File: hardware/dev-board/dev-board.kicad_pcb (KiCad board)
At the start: 4 copper layers, 66 x 119.3 mm, 150 parts, among them IC201 ADV7393BCPZ, J101 Conn_01x02_Pin, J102 DISC1-P1, J103 DISC1-P2, J201 CVBS, J301 Connector RGB, U101 MCP2562-E-SN, U102 CDCE913PW, U103 AMS1117-1.8, U301 ADV7125KSTZ140

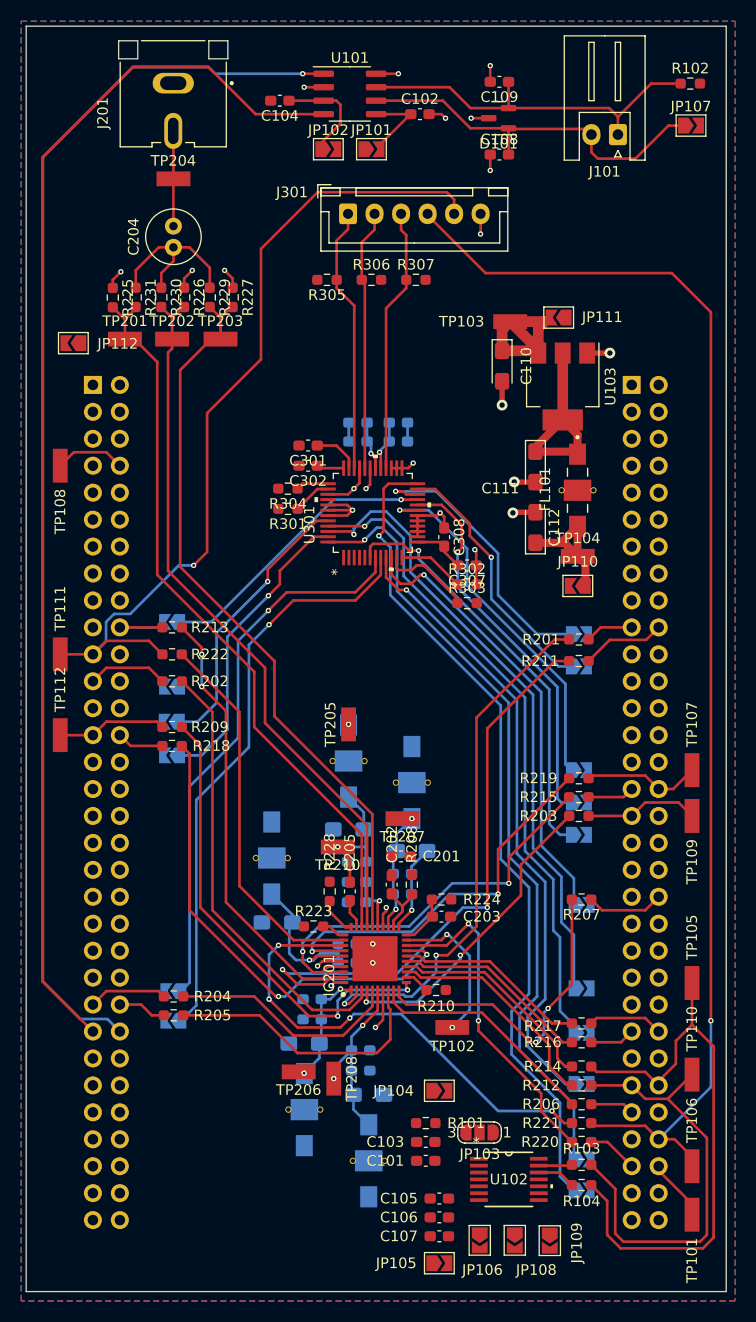
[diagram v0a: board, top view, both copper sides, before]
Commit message: adv7393 dev-board done
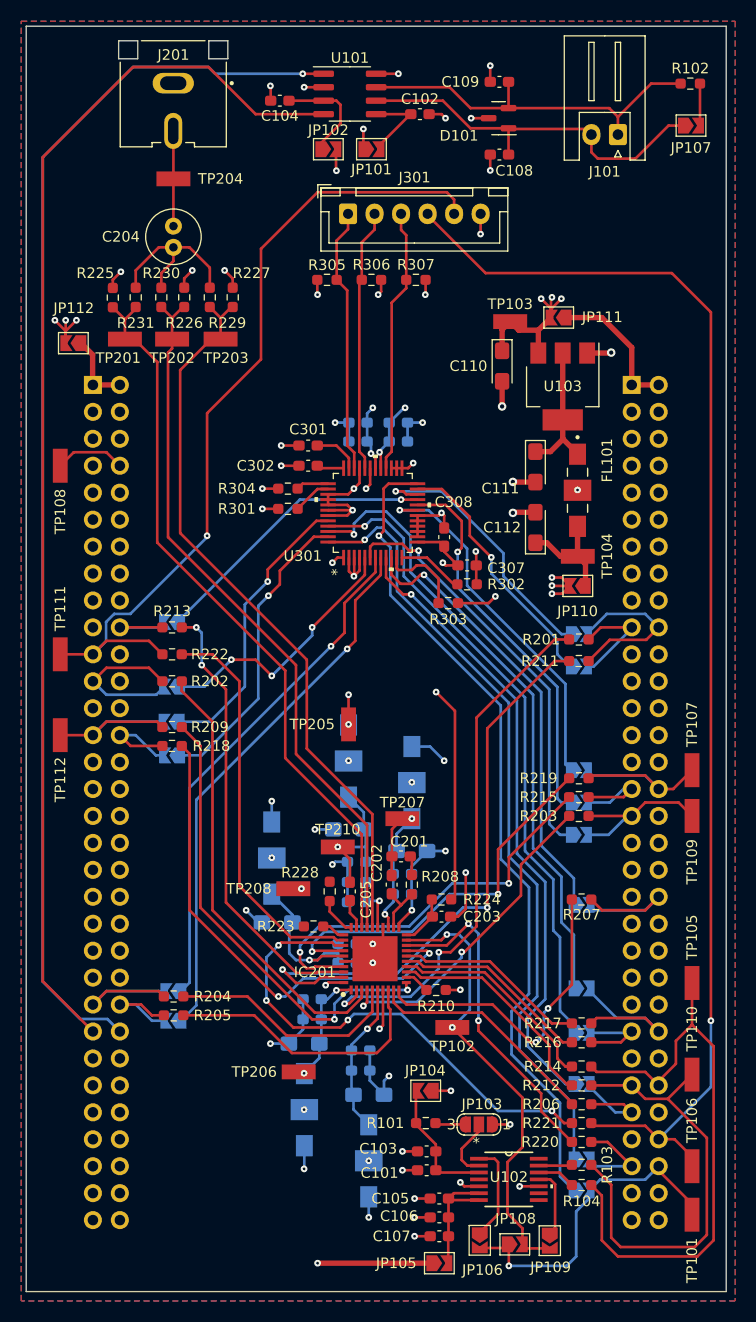
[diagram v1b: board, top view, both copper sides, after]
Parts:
- moved TP208 18.3 mm to (75.2, 131.3), turned to 0 degrees
- moved R303 1.78 mm to (89.8, 104.4)
- moved JP104 1.29 mm to (87.7, 150.4), turned to 180 degrees
- moved C103 0.89 mm to (87.8, 156.1)
- moved C101 0.89 mm to (87.8, 157.9)
- moved JP103 0.76 mm to (92.7, 153.5)
- moved JP108 0.38 mm to (96.1, 164.8), turned to 0 degrees
- turned R101 to 0 degrees
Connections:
- C209 pad 1: DVDD_1V8 -> DVDD_1V8_2
- C210 pad 1: DVDD_1V8 -> DVDD_1V8_1
- C214 pad 1: DVDD_1V8 -> DVDD_1V8_2
- C215 pad 1: DVDD_1V8 -> DVDD_1V8_1
- C219 pad 1: DVDD_1V8 -> DVDD_1V8_2
- C220 pad 1: DVDD_1V8 -> DVDD_1V8_1
- FL204 pad 3: DVDD_1V8 -> DVDD_1V8_2
- FL205 pad 3: DVDD_1V8 -> DVDD_1V8_1
- IC201 pad 35: DVDD_1V8 -> DVDD_1V8_2
- IC201 pad 6: DVDD_1V8 -> DVDD_1V8_1
- R224 pad 2: DVDD_IO_3V3 -> +3V3
- TP208 pad 1: DVDD_1V8 -> DVDD_1V8_2
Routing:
- net GND: track 77.5 -> 141.4 mm, vias 27 -> 56
- net +3V3: track 0.00 -> 44.3 mm, vias 1 -> 9
- net DVDD_1V8: track 34.6 -> 0.00 mm, vias 3 -> 0
- net ADV_CLKIN: track 14.5 -> 42.1 mm
- net LTDC_CLK: track 5.88 -> 31.6 mm, vias 0 -> 1
- net ADV7_G2: track 0.00 -> 25.2 mm, vias 0 -> 3
- net DVDD_1V8_2: track 0.00 -> 19.8 mm, vias 0 -> 2
- net +5V: track 31.4 -> 46.5 mm, vias 2 -> 13
- net +1V8: track 0.00 -> 14.9 mm, vias 0 -> 7
- net DVDD_1V8_1: track 0.00 -> 14.4 mm, vias 0 -> 1
- net +5V_IN: track 0.00 -> 13.4 mm
- net +1V8_I: track 0.00 -> 12.5 mm
- net +3V3_I: track 0.00 -> 12.2 mm
- net Net-(JP106-A): track 0.00 -> 9.29 mm
- net LTDC_R5: track 7.09 -> 15.4 mm
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- added copper zone on In2.Cu, net +1V8
- added copper zone on In2.Cu, net +3V3
- added copper zone on In2.Cu, net +5V
- removed copper zone on In1.Cu, net +3V3

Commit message: production
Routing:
- net GND: vias 56 -> 220
